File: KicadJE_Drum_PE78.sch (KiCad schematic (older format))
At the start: 50 parts

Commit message: Breadboard sch
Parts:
- gave numbers to parts that had none: 44
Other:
- moved on the sheet: U101E, U101F

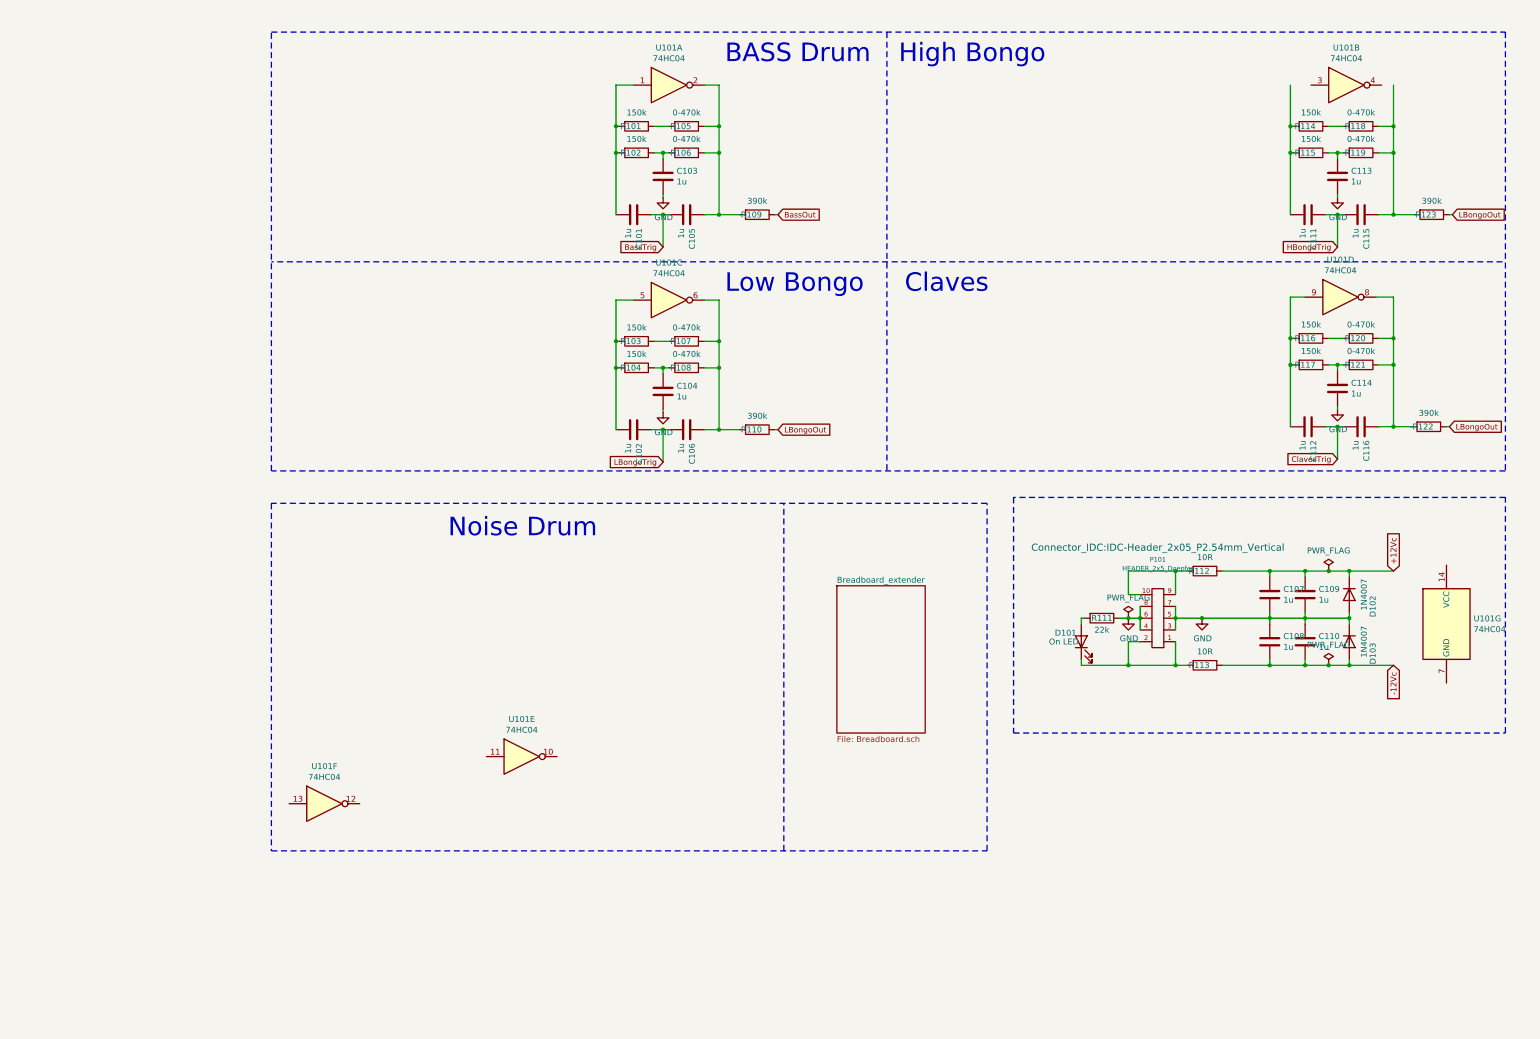
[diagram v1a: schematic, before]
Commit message: Sinus osc done - sch
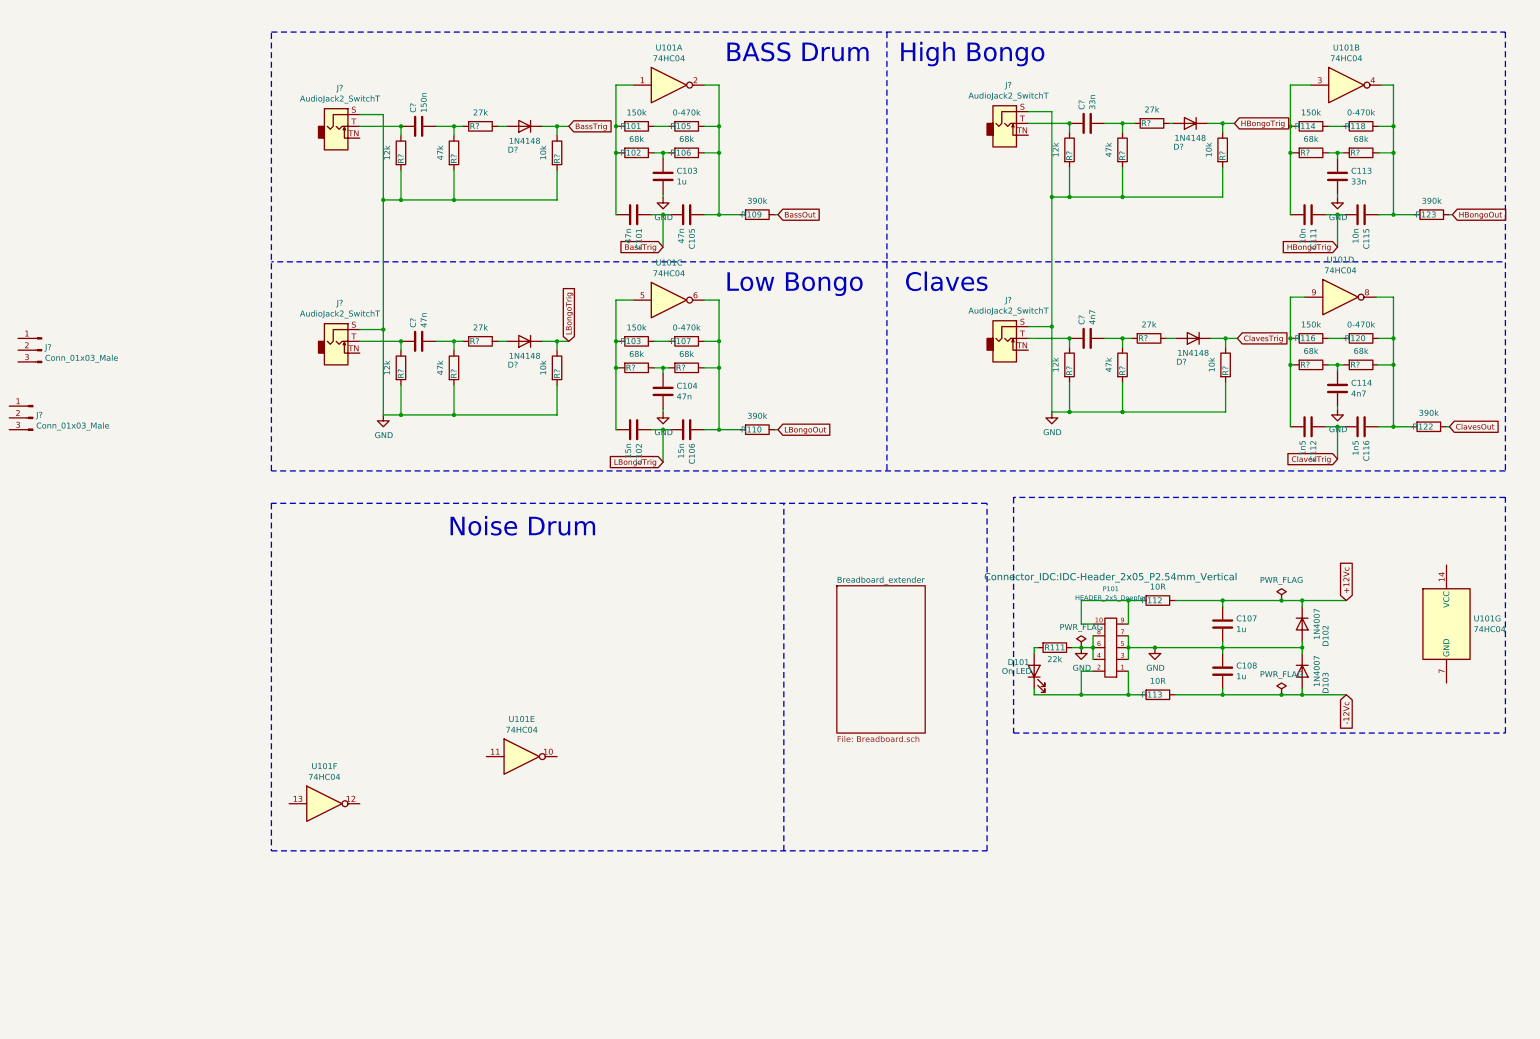
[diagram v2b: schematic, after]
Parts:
- removed C109, C110: 1u, AJ:C_0805_AJ, symbol Device:C
- removed R104, R115, R117: 150k, AJ:R_0805_AJ, symbol Device:R
- removed R108, R119, R121: 0-470k, AJ:R_0805_AJ, symbol Device:R
- added C?: 150n, Capacitor_SMD:C_1206_3216Metric_Pad1.42x1.75mm_HandSolder, symbol Device:C
- added C?: 33n, Capacitor_SMD:C_1206_3216Metric_Pad1.42x1.75mm_HandSolder, symbol Device:C
- added C?: 47n, Capacitor_SMD:C_1206_3216Metric_Pad1.42x1.75mm_HandSolder, symbol Device:C
- added C?: 4n7, Capacitor_SMD:C_1206_3216Metric_Pad1.42x1.75mm_HandSolder, symbol Device:C
- added D? (x4): 1N4148, Diode_SMD:D_MiniMELF, symbol Diode:LL4148
- added J? (x2): Conn_01x03_Male, Connector_PinHeader_2.54mm:PinHeader_1x03_P2.54mm_Vertical, symbol Connector:Conn_01x03_Male
- added J? (x4): AudioJack2_SwitchT, Connector_Audio:Jack_3.5mm_QingPu_WQP-PJ398SM_Vertical_CircularHoles, symbol Connector:AudioJack2_SwitchT
- added R? (x4): 47k, AJ:R_0805_AJ, symbol Device:R
- added R? (x4): 12k, AJ:R_0805_AJ, symbol Device:R
- added R? (x4): 10k, AJ:R_0805_AJ, symbol Device:R
- added R? (x4): 27k, AJ:R_0805_AJ, symbol Device:R
- added R? (x6): 68k, AJ:R_0805_AJ, symbol Device:R
- C101, C104, C105: value 1u -> 47n
- C102, C106: value 1u -> 15n
- C111, C115: value 1u -> 10n
- C112, C116: value 1u -> 1n5
- C113: value 1u -> 33n
- C114: value 1u -> 4n7
- R102: value 150k -> 68k
- R106: value 0-470k -> 68k
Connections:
- net BassTrig: now also D?.1 (K), R?.1
- net ClavesTrig: now also D?.1 (K), R?.1
- net GND: now also J?.S, J?.S, J?.S, J?.S, R?.2, R?.2, R?.2, R?.2, R?.2, R?.2, R?.2, R?.2, R?.2, R?.2, R?.2, R?.2
- net HBongoTrig: now also D?.1 (K), R?.1
- net LBongoOut: no longer R122.1, R123.1
- net LBongoTrig: now also D?.1 (K), R?.1
- net at U101.3: now also C111.2, R114.2, R?.2
- net at U101.4: now also C115.1, R118.1, R123.2, R?.1
- net at C102.2, R103.2, U101.5: now also R?.2
- net at C106.1, R107.1, R110.2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: now also R?.1
- net at C116.1, R120.1, R122.2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: now also R?.1
- net at C112.2, R116.2, U101.9: now also R?.2
- net at C113.1: now also R?.1, R?.2
- net at C114.1: now also R?.1, R?.2
- net at C104.1: now also R?.1, R?.2
- new net: C?.1, J?.T, R?.1 (x4)
- new net: C?.2, R?.1, R?.2 (x4)
- new net: D?.2 (A), R?.1 (x4)
- new net ClavesOut: R122.1
- new net HBongoOut: R123.1
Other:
- moved on the sheet: C107, C108, D101, D102, D103, P101, R111, R112, R113

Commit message: Noise drums
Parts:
- removed J? (x2): Conn_01x03_Male, Connector_PinHeader_2.54mm:PinHeader_1x03_P2.54mm_Vertical, symbol Connector:Conn_01x03_Male
- removed P101: HEADER_2x5_Doepfer, Connector_IDC:IDC-Header_2x05_P2.54mm_Vertical, symbol Eurorack:HEADER_2x5_Doepfer
- removed R107, R118, R120: 0-470k, AJ:R_0805_AJ, symbol Device:R
- removed unit 5 of U101
- removed unit 6 of U101
- added C? (x3): 100n, Capacitor_SMD:C_1206_3216Metric_Pad1.42x1.75mm_HandSolder, symbol Device:C
- added C?: 330n, Capacitor_SMD:C_1206_3216Metric_Pad1.42x1.75mm_HandSolder, symbol Device:C
- added C? (x2): 68n, Capacitor_SMD:C_1206_3216Metric_Pad1.42x1.75mm_HandSolder, symbol Device:C
- added C?: 220n, Capacitor_SMD:C_1206_3216Metric_Pad1.42x1.75mm_HandSolder, symbol Device:C
- added C? (x2): 4n7, Capacitor_SMD:C_1206_3216Metric_Pad1.42x1.75mm_HandSolder, symbol Device:C
- added C?: 22n, Capacitor_SMD:C_1206_3216Metric_Pad1.42x1.75mm_HandSolder, symbol Device:C
- added D? (x4): 1N4148, Diode_SMD:D_MiniMELF, symbol Diode:LL4148
- added J?: Snare, Connector_Audio:Jack_3.5mm_QingPu_WQP-PJ398SM_Vertical_CircularHoles, symbol Connector:AudioJack2_SwitchT
- added J?: LCymbals, Connector_Audio:Jack_3.5mm_QingPu_WQP-PJ398SM_Vertical_CircularHoles, symbol Connector:AudioJack2_SwitchT
- added J?: SCymbals, Connector_Audio:Jack_3.5mm_QingPu_WQP-PJ398SM_Vertical_CircularHoles, symbol Connector:AudioJack2_SwitchT
- added J?: Maracas, Connector_Audio:Jack_3.5mm_QingPu_WQP-PJ398SM_Vertical_CircularHoles, symbol Connector:AudioJack2_SwitchT
- added L? (x2): 100mH, Inductor_THT:L_Radial_D7.5mm_P3.50mm_Fastron_07P, symbol Device:L
- added L? (x2): 100mH, Inductor_SMD:L_1206_3216Metric, symbol Device:L
- added Q? (x4): 2N3904, Package_TO_SOT_SMD:SOT-23_Handsoldering, symbol Transistor_BJT:2N3904
- added R? (x3): 0-470k, AJ:R_0805_AJ, symbol Device:R
- added R? (x3): 22k, AJ:R_0805_AJ, symbol Device:R
- added R? (x2): 10k, AJ:R_0805_AJ, symbol Device:R
- added R? (x5): 1M, AJ:R_0805_AJ, symbol Device:R
- added R?: 100k, AJ:R_0805_AJ, symbol Device:R
- added R?: 470k, AJ:R_0805_AJ, symbol Device:R
- added R?: 2k2, AJ:R_0805_AJ, symbol Device:R
- added R? (x2): 4k7, AJ:R_0805_AJ, symbol Device:R
- added RV?: R_POT_TRIM, symbol Device:R_POT_TRIM
- added RV?: R_POT, symbol Device:R_POT
- C103: value 1u -> 150n
- J?: value AudioJack2_SwitchT -> Bass
- J?: value AudioJack2_SwitchT -> LBongo
- J?: value AudioJack2_SwitchT -> HBongo
- J?: value AudioJack2_SwitchT -> Claves
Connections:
- net +12Vc: now also L?.1, L?.1, L?.1, L?.1, R?.2, R?.2, RV?.1; no longer R112.1
- net GND: now also U101.7 (GND), C?.2, C?.2, C?.2, C?.2, C?.2, D?.2 (A), J?.S, J?.S, J?.S, J?.S, Q?.1 (E), Q?.1 (E), Q?.2 (B), R?.1, R?.1, R?.1, R?.2, R?.2
- net LBongoTrig: now also D?.1 (K)
- net at C115.1, R123.2, R?.1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: now also R?.1
- net at C106.1, R110.2, R?.1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: now also R?.1
- net at C116.1, R122.2, R?.1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: now also R?.1
- net +5V: now reaches U101.14 (VCC)
- net +5V: now also Q?.3 (C)
- net at R114.1: now also R?.2
- net at R116.1: now also R?.2
- net at R103.1: now also R?.2
- new net: C?.1, D?.2 (A), J?.T
- new net: J?.TN, J?.TN, J?.TN, R?.2
- new net: C?.2, Q?.2 (B), R?.1
- new net: C?.1, J?.T, R?.2
- new net: J?.T, R?.2
- new net: C?.1, J?.T, R?.1
- new net: D?.2 (A), Q?.1 (E)
- new net: C?.1, R?.1, R?.2 (x3)
- new net: C?.1, Q?.2 (B), R?.1, R?.1, R?.1, R?.2
- new net: C?.2, D?.1 (K), D?.2 (A)
- new net: D?.1 (K), R?.2 (x2)
- new net: C?.2, Q?.2 (B), R?.1, R?.2
- new net: Q?.1 (E), RV?.3
- new net: L?.2, L?.2, Q?.3 (C), R?.1, RV?.3
- new net: C?.1, L?.2, L?.2, Q?.3 (C), R?.1, RV?.1
- new net: C?.1, R?.1
- new net: R?.2, RV?.2
- new net NDrumsOut: C?.2
- new net NoiseOut: C?.1, C?.2, RV?.2
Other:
- note added: "HUSK NU AT LAVE +5V !!!!!!!!!!"
- moved on the sheet: C101, C102, C103, C104, C105, C106, C111, C112, C113, C114, C115, C116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
